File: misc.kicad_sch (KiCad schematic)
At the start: 12 parts

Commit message: commit before updating to LiveAstra lib
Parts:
- removed H1, H2, H3, H4: MountingHole_Pad, MountingHole:MountingHole_5.3mm_M5_DIN965_Pad, symbol EASYEDA2KICAD:MountingHole_Pad
- added G1: ~, EASYEDA2KICAD:AstraControl_Ground_Band, symbol EASYEDA2KICAD:AstraControl_Ground_Guard
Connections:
- net CHASSIS: now also G1.1 (2)

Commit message: Updated library name, updated and verified all footprints
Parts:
- C23, C24, C25, C26: symbol EASYEDA2KICAD:C_10nF_X7R_0805 -> LiveAstra:C_10nF_X7R_0805
- G1: footprint EASYEDA2KICAD:AstraControl_Ground_Band -> LiveAstra:AstraControl_Ground_Band; symbol EASYEDA2KICAD:AstraControl_Ground_Guard -> LiveAstra:AstraControl_Ground_Guard; now in the parts list
- R34, R35, R36, R37: symbol EASYEDA2KICAD:R_1MOhm_0805_125mW -> LiveAstra:R_1MOhm_0805_125mW
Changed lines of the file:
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@@
 	)
 	(symbol
-		(lib_id "EASYEDA2KICAD:R_1MOhm_0805_125mW")
+		(lib_id "LiveAstra:R_1MOhm_0805_125mW")
 		(at 187.96 83.82 90)
 		(unit 1)
@@
 	)
 	(symbol
-		(lib_id "EASYEDA2KICAD:R_1MOhm_0805_125mW")
+		(lib_id "LiveAstra:R_1MOhm_0805_125mW")
 		(at 88.9 83.82 90)
 		(unit 1)
@@
 	)
 	(symbol
-		(lib_id "EASYEDA2KICAD:R_1MOhm_0805_125mW")
+		(lib_id "LiveAstra:R_1MOhm_0805_125mW")
 		(at 236.22 83.82 90)
 		(unit 1)
@@
 	)
 	(symbol
-		(lib_id "EASYEDA2KICAD:C_10nF_X7R_0805")
+		(lib_id "LiveAstra:C_10nF_X7R_0805")
 		(at 167.64 83.82 90)
 		(unit 1)
@@
 	)
 	(symbol
-		(lib_id "EASYEDA2KICAD:CHASSIS")
+		(lib_id "LiveAstra:CHASSIS")
 		(at 55.88 96.52 0)
 		(unit 1)
@@
 	)
 	(symbol
-		(lib_id "EASYEDA2KICAD:R_1MOhm_0805_125mW")
+		(lib_id "LiveAstra:R_1MOhm_0805_125mW")
 		(at 139.7 83.82 90)
 		(unit 1)
@@
 	)
 	(symbol
-		(lib_id "EASYEDA2KICAD:C_10nF_X7R_0805")
+		(lib_id "LiveAstra:C_10nF_X7R_0805")
 		(at 68.58 83.82 90)
 		(unit 1)
@@
 	)
 	(symbol
-		(lib_id "EASYEDA2KICAD:C_10nF_X7R_0805")
+		(lib_id "LiveAstra:C_10nF_X7R_0805")
 		(at 215.9 83.82 90)
 		(unit 1)
@@
 	)
 	(symbol
-		(lib_id "EASYEDA2KICAD:AstraControl_Ground_Guard")
+		(lib_id "LiveAstra:AstraControl_Ground_Guard")
 		(at 55.88 66.04 0)
 		(unit 1)
 		(exclude_from_sim no)
-		(in_bom no)
+		(in_bom yes)
 		(on_board yes)
 		(dnp no)
@@
 			)
 		)
-		(property "Footprint" "EASYEDA2KICAD:AstraControl_Ground_Band"
+		(property "Footprint" "LiveAstra:AstraControl_Ground_Band"
 			(at 55.88 59.69 0)
 			(effects
@@
 	)
 	(symbol
-		(lib_id "EASYEDA2KICAD:C_10nF_X7R_0805")
+		(lib_id "LiveAstra:C_10nF_X7R_0805")
 		(at 119.38 83.82 90)
 		(unit 1)

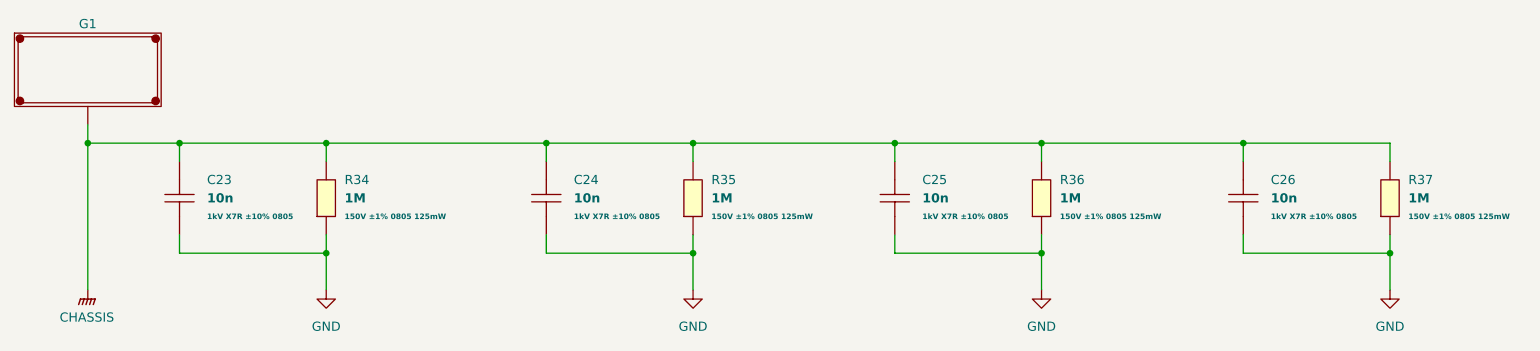
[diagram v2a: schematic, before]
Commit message: Finished layout no drc or erc errors
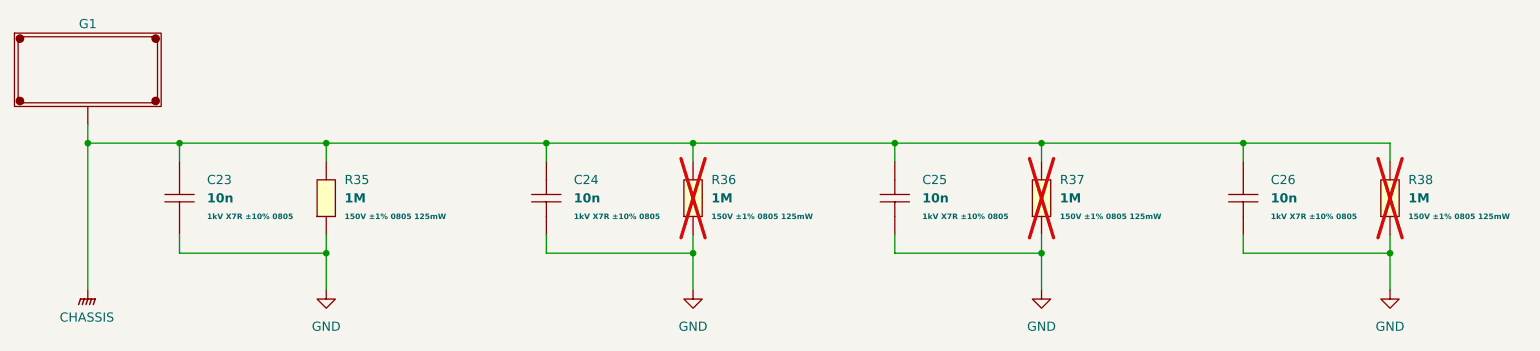
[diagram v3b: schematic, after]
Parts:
- C23, C24, C25, C26: footprint Capacitor_SMD:C_0805_2012Metric_Pad1.18x1.45mm_HandSolder -> LiveAstra:C_0805_2012Metric_Pad1.18x1.45mm_HandSolder
- R35: renamed from R34; footprint Resistor_SMD:R_0805_2012Metric_Pad1.20x1.40mm_HandSolder -> LiveAstra:R_0805_2012Metric_Pad1.20x1.40mm_HandSolder
- R36: renamed from R35; footprint Resistor_SMD:R_0805_2012Metric_Pad1.20x1.40mm_HandSolder -> LiveAstra:R_0805_2012Metric_Pad1.20x1.40mm_HandSolder; now not fitted
- R37: renamed from R36; footprint Resistor_SMD:R_0805_2012Metric_Pad1.20x1.40mm_HandSolder -> LiveAstra:R_0805_2012Metric_Pad1.20x1.40mm_HandSolder; now not fitted
- R38: renamed from R37; footprint Resistor_SMD:R_0805_2012Metric_Pad1.20x1.40mm_HandSolder -> LiveAstra:R_0805_2012Metric_Pad1.20x1.40mm_HandSolder; now not fitted
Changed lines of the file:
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@@
 		(dnp no)
 		(fields_autoplaced yes)
-		(property "Reference" "#PWR091"
+		(property "Reference" "#PWR088"
 			(at 236.22 102.87 0)
 			(effects
@@
 			(project "AstraControl"
 				(path "/9a751838-dce8-4d69-8a02-736625ac74e7/0db21d8e-3390-4d67-877f-0e5d98e37848/f4845962-3a2f-4778-bb13-eae0f2a437f4"
-					(reference "#PWR091")
+					(reference "#PWR088")
 					(unit 1)
 				)
@@
 		(in_bom yes)
 		(on_board yes)
-		(dnp no)
-		(fields_autoplaced yes)
-		(property "Reference" "R36"
+		(dnp yes)
+		(fields_autoplaced yes)
+		(property "Reference" "R37"
 			(at 190.5 81.2799 90)
 			(effects
@@
 			)
 		)
-		(property "Footprint" "Resistor_SMD:R_0805_2012Metric_Pad1.20x1.40mm_HandSolder"
+		(property "Footprint" "LiveAstra:R_0805_2012Metric_Pad1.20x1.40mm_HandSolder"
 			(at 196.85 83.82 0)
 			(effects
@@
 			(project "AstraControl"
 				(path "/9a751838-dce8-4d69-8a02-736625ac74e7/0db21d8e-3390-4d67-877f-0e5d98e37848/f4845962-3a2f-4778-bb13-eae0f2a437f4"
-					(reference "R36")
+					(reference "R37")
 					(unit 1)
 				)
@@
 		(dnp no)
 		(fields_autoplaced yes)
-		(property "Reference" "R34"
+		(property "Reference" "R35"
 			(at 91.44 81.2799 90)
 			(effects
@@
 			)
 		)
-		(property "Footprint" "Resistor_SMD:R_0805_2012Metric_Pad1.20x1.40mm_HandSolder"
+		(property "Footprint" "LiveAstra:R_0805_2012Metric_Pad1.20x1.40mm_HandSolder"
 			(at 97.79 83.82 0)
 			(effects
@@
 			(project ""
 				(path "/9a751838-dce8-4d69-8a02-736625ac74e7/0db21d8e-3390-4d67-877f-0e5d98e37848/f4845962-3a2f-4778-bb13-eae0f2a437f4"
-					(reference "R34")
+					(reference "R35")
 					(unit 1)
 				)
@@
 		(in_bom yes)
 		(on_board yes)
-		(dnp no)
-		(fields_autoplaced yes)
-		(property "Reference" "R37"
+		(dnp yes)
+		(fields_autoplaced yes)
+		(property "Reference" "R38"
 			(at 238.76 81.2799 90)
 			(effects
@@
 			)
 		)
-		(property "Footprint" "Resistor_SMD:R_0805_2012Metric_Pad1.20x1.40mm_HandSolder"
+		(property "Footprint" "LiveAstra:R_0805_2012Metric_Pad1.20x1.40mm_HandSolder"
 			(at 245.11 83.82 0)
 			(effects
@@
 			(project "AstraControl"
 				(path "/9a751838-dce8-4d69-8a02-736625ac74e7/0db21d8e-3390-4d67-877f-0e5d98e37848/f4845962-3a2f-4778-bb13-eae0f2a437f4"
-					(reference "R37")
+					(reference "R38")
 					(unit 1)
 				)
@@
 			)
 		)
-		(property "Footprint" "Capacitor_SMD:C_0805_2012Metric_Pad1.18x1.45mm_HandSolder"
+		(property "Footprint" "LiveAstra:C_0805_2012Metric_Pad1.18x1.45mm_HandSolder"
 			(at 176.53 83.82 0)
 			(effects
@@
 		(in_bom yes)
 		(on_board yes)
-		(dnp no)
-		(fields_autoplaced yes)
-		(property "Reference" "R35"
+		(dnp yes)
+		(fields_autoplaced yes)
+		(property "Reference" "R36"
 			(at 142.24 81.2799 90)
 			(effects
@@
 			)
 		)
-		(property "Footprint" "Resistor_SMD:R_0805_2012Metric_Pad1.20x1.40mm_HandSolder"
+		(property "Footprint" "LiveAstra:R_0805_2012Metric_Pad1.20x1.40mm_HandSolder"
 			(at 148.59 83.82 0)
 			(effects
@@
 			(project "AstraControl"
 				(path "/9a751838-dce8-4d69-8a02-736625ac74e7/0db21d8e-3390-4d67-877f-0e5d98e37848/f4845962-3a2f-4778-bb13-eae0f2a437f4"
-					(reference "R35")
+					(reference "R36")
 					(unit 1)
 				)
@@
 		(dnp no)
 		(fields_autoplaced yes)
-		(property "Reference" "#PWR087"
+		(property "Reference" "#PWR086"
 			(at 139.7 102.87 0)
 			(effects
@@
 			(project "AstraControl"
 				(path "/9a751838-dce8-4d69-8a02-736625ac74e7/0db21d8e-3390-4d67-877f-0e5d98e37848/f4845962-3a2f-4778-bb13-eae0f2a437f4"
-					(reference "#PWR087")
+					(reference "#PWR086")
 					(unit 1)
 				)
@@
 			)
 		)
-		(property "Footprint" "Capacitor_SMD:C_0805_2012Metric_Pad1.18x1.45mm_HandSolder"
+		(property "Footprint" "LiveAstra:C_0805_2012Metric_Pad1.18x1.45mm_HandSolder"
 			(at 77.47 83.82 0)
 			(effects
@@
 			)
 		)
-		(property "Footprint" "Capacitor_SMD:C_0805_2012Metric_Pad1.18x1.45mm_HandSolder"
+		(property "Footprint" "LiveAstra:C_0805_2012Metric_Pad1.18x1.45mm_HandSolder"
 			(at 224.79 83.82 0)
 			(effects
@@
 		(dnp no)
 		(fields_autoplaced yes)
-		(property "Reference" "#PWR089"
+		(property "Reference" "#PWR087"
 			(at 187.96 102.87 0)
 			(effects
@@
 			(project "AstraControl"
 				(path "/9a751838-dce8-4d69-8a02-736625ac74e7/0db21d8e-3390-4d67-877f-0e5d98e37848/f4845962-3a2f-4778-bb13-eae0f2a437f4"
-					(reference "#PWR089")
+					(reference "#PWR087")
 					(unit 1)
 				)
@@
 			)
 		)
-		(property "Footprint" "Capacitor_SMD:C_0805_2012Metric_Pad1.18x1.45mm_HandSolder"
+		(property "Footprint" "LiveAstra:C_0805_2012Metric_Pad1.18x1.45mm_HandSolder"
 			(at 128.27 83.82 0)
 			(effects

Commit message: workflow
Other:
- title: (none) -> Miscellaneous
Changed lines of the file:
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@@
 	(generator_version "8.0")
 	(paper "A4")
+	(title_block
+		(title "Miscellaneous")
+	)
 	(junction
 		(at 167.64 76.2)
